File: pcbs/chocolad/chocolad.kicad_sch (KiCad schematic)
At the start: 68 parts, among them J1 TRRS, J2 OLED, SW1 SW_PUSH, SW10 SW_PUSH, SW11 SW_PUSH, SW12 SW_PUSH, SW13 SW_PUSH, SW14 SW_PUSH, SW15 SW_PUSH, SW16 SW_PUSH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

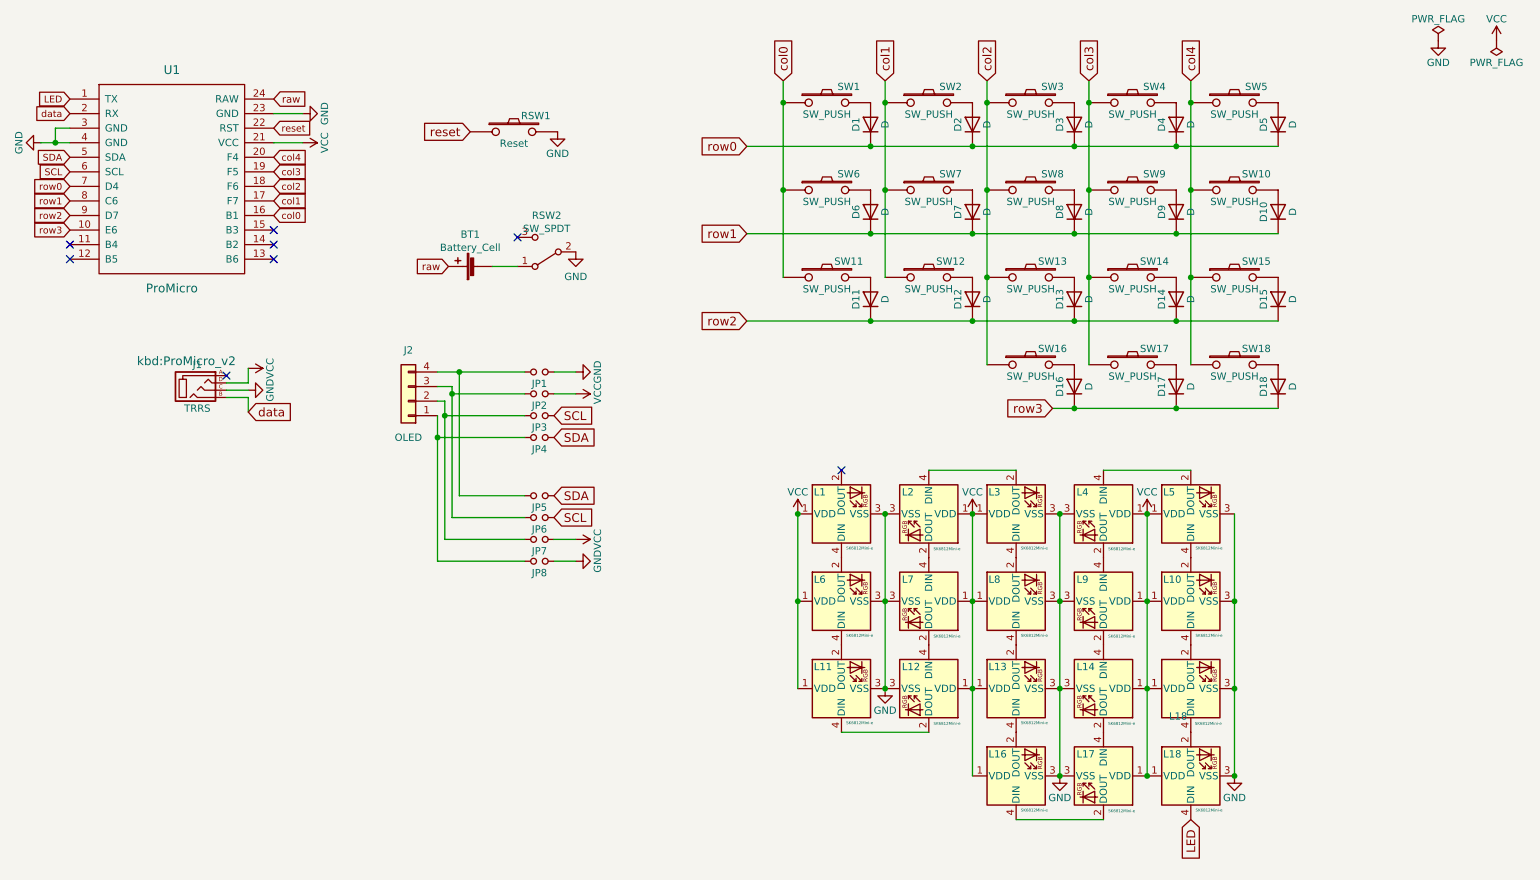
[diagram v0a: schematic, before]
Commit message: Added and changed components and altered shape.
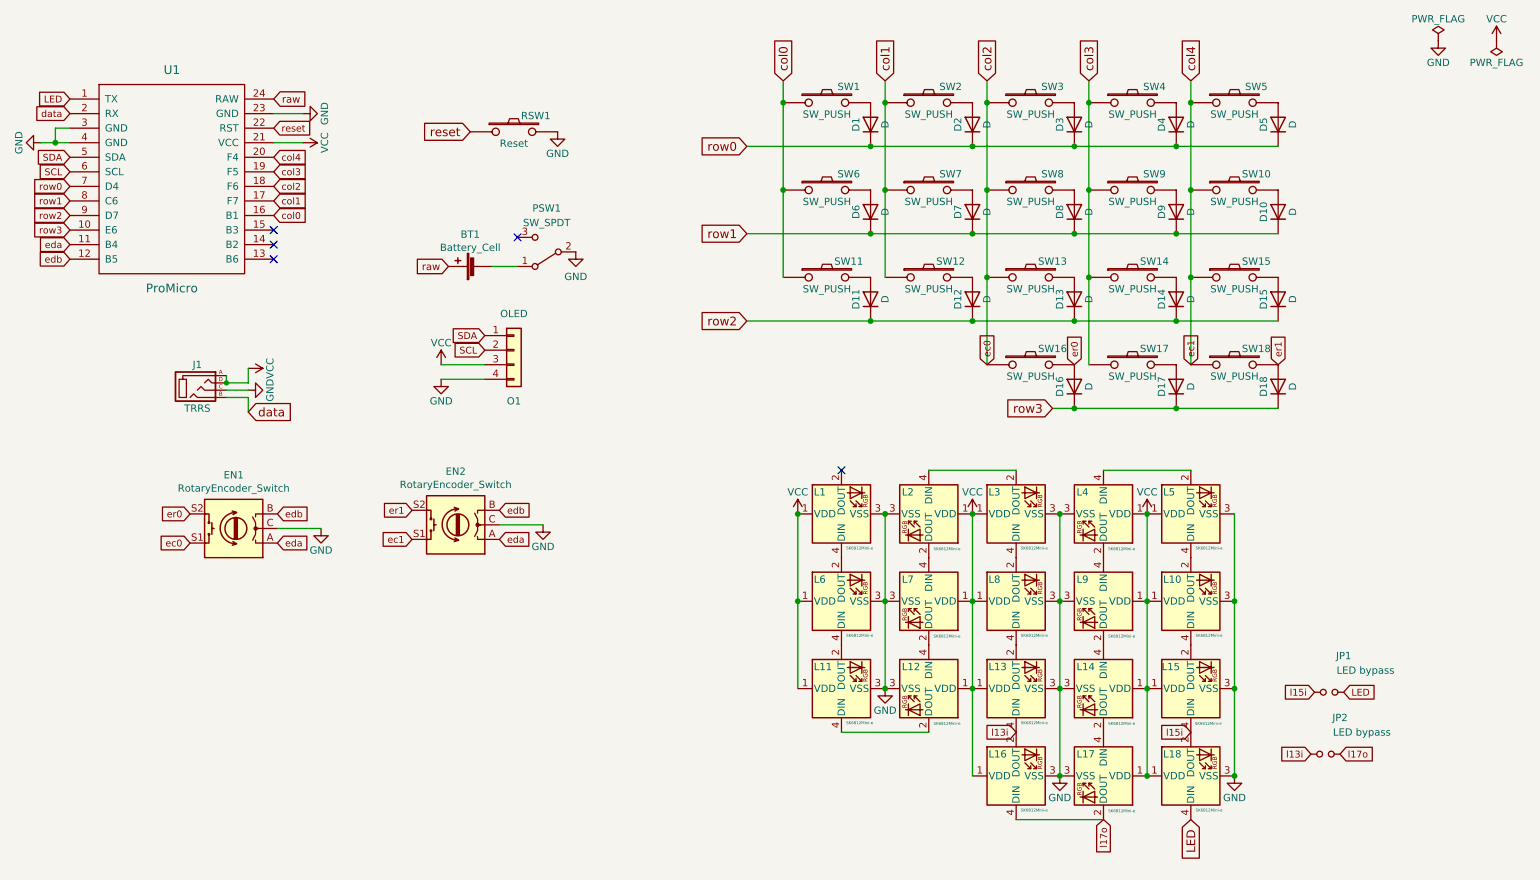
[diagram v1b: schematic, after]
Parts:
- removed J2: OLED, kbd:OLED, symbol Connector_Generic:Conn_01x04
- removed JP3, JP4, JP5, JP6, JP7, JP8: (no value), kbd:Jumper, symbol Device:Jumper_NO_Small
- added EN1, EN2: RotaryEncoder_Switch, swoop:RotaryEncoder, symbol Device:RotaryEncoder_Switch
- added O1: OLED, swoop:OLED_jumpers, symbol Connector_Generic:Conn_01x04
- JP1, JP2: value (none) -> LED bypass; footprint kbd:Jumper -> swoop:Jumper
- renumbered L18 to L15, RSW2 to PSW1
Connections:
- net GND: now also EN1.C, EN2.C, O1.4 (Pin_4); no longer JP1.1
- net LED: now also JP1.1
- net SCL: now also O1.2 (Pin_2)
- net SDA: now also O1.1 (Pin_1)
- net VCC: now also J1.A, O1.3 (Pin_3); no longer JP2.1
- net col2: now also EN1.S1
- net col4: now also EN2.S1
- net eda: now reaches U1.11 (B4)
- net eda: now also EN1.A, EN2.A
- net edb: now reaches U1.12 (B5)
- net edb: now also EN1.B, EN2.B
- net er1: now reaches D18.2 (A), SW18.2
- net er1: now also EN2.S2
- net er0: now reaches D16.2 (A), SW16.2
- net er0: now also EN1.S2
- net l13i: now reaches JP2.2
- net l13i: now also L13.4 (DIN), L16.2 (DOUT)
- net l15i: now reaches JP1.2
- net l15i: now also L15.4 (DIN), L18.2 (DOUT)
- net l17o: now reaches L16.4 (DIN), L17.2 (DOUT)
- net l17o: now also JP2.1
- no-connect marks 8 -> 5

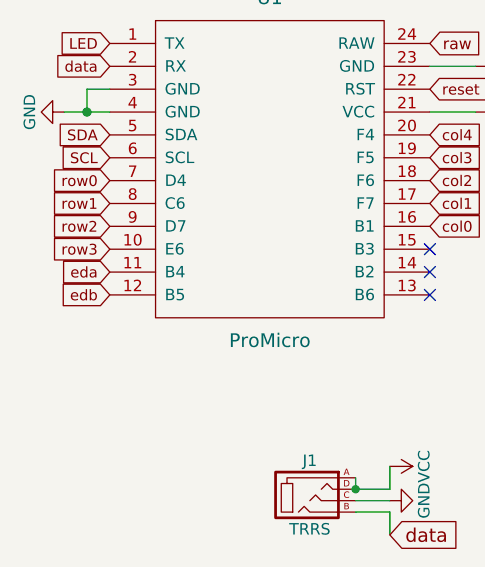
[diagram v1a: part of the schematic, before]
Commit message: Finalised traces.
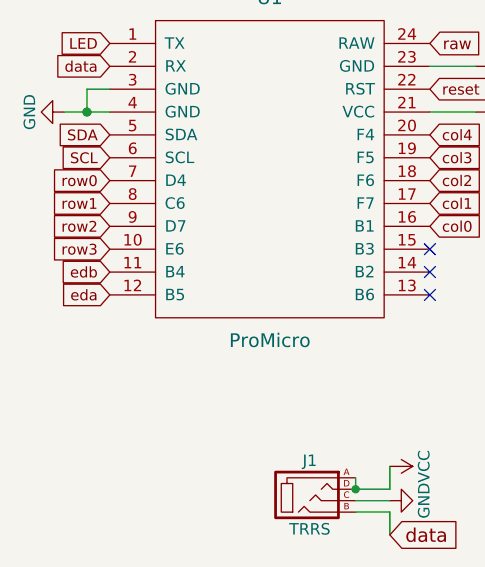
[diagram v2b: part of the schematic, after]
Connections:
- net eda: now also U1.12 (B5); no longer U1.11 (B4)
- net edb: now also U1.11 (B4); no longer U1.12 (B5)
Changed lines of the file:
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@@
     )
   )
-  (global_label "eda" (shape input) (at 27.94 55.88 180) (fields_autoplaced)
+  (global_label "eda" (shape input) (at 27.94 58.42 180) (fields_autoplaced)
     (effects (font (size 1.1938 1.1938)) (justify right))
-    (property "Intersheet References" "${INTERSHEET_REFS}" (id 0) (at 22.5719 55.9546 0)
+    (property "Intersheet References" "${INTERSHEET_REFS}" (id 0) (at 22.5719 58.4946 0)
       (effects (font (size 1.1938 1.1938)) (justify right) hide)
     )
@@
     )
   )
-  (global_label "edb" (shape input) (at 27.94 58.42 180) (fields_autoplaced)
+  (global_label "edb" (shape input) (at 27.94 55.88 180) (fields_autoplaced)
     (effects (font (size 1.1938 1.1938)) (justify right))
-    (property "Intersheet References" "${INTERSHEET_REFS}" (id 0) (at 22.5719 58.4946 0)
+    (property "Intersheet References" "${INTERSHEET_REFS}" (id 0) (at 22.5719 55.9546 0)
       (effects (font (size 1.1938 1.1938)) (justify right) hide)
     )

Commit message: Moved footprints into local library.
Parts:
- BT1: footprint jmnw:Battery_pads_reversible -> chocolad:Battery_pads
- D1, D10, D11, D12, D13, D14, D15, D16, D17, D18, D2, D3, D4, D5, D6, D7, D8, D9: footprint kbd:D3_TH_SMD -> chocolad:D3_SMD
- EN1, EN2: footprint swoop:RotaryEncoder -> chocolad:RotaryEncoder
- J1: footprint kbd:MJ-4PP-9 -> chocolad:TRRS
- JP1, JP2: footprint swoop:Jumper -> chocolad:Jumper
- L1, L10, L11, L12, L13, L14, L15, L16, L17, L18, L2, L3, L4, L5, L6, L7, L8, L9: footprint jmnw:sk6812_mini_e_rev -> chocolad:SK6812_Mini_E
- O1: footprint swoop:OLED_jumpers -> chocolad:OLED
- PSW1: footprint jmnw:Power_reversible -> chocolad:Power
- RSW1: footprint kbd:ResetSW -> chocolad:Reset
- SW1, SW10, SW11, SW12, SW13, SW14, SW15, SW16, SW17, SW18, SW2, SW3, SW4, SW5, SW6, SW7, SW8, SW9: footprint jmnw:Choc_reversible -> chocolad:Choc
- U1: footprint kbd:ProMicro_v2 -> chocolad:ProMicro
